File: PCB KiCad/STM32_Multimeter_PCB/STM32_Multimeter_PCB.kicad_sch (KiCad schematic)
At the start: 18 parts, among them SW1 SW_Push, U1 STM32WB55CGUx, Y1 Crystal 32 MHz

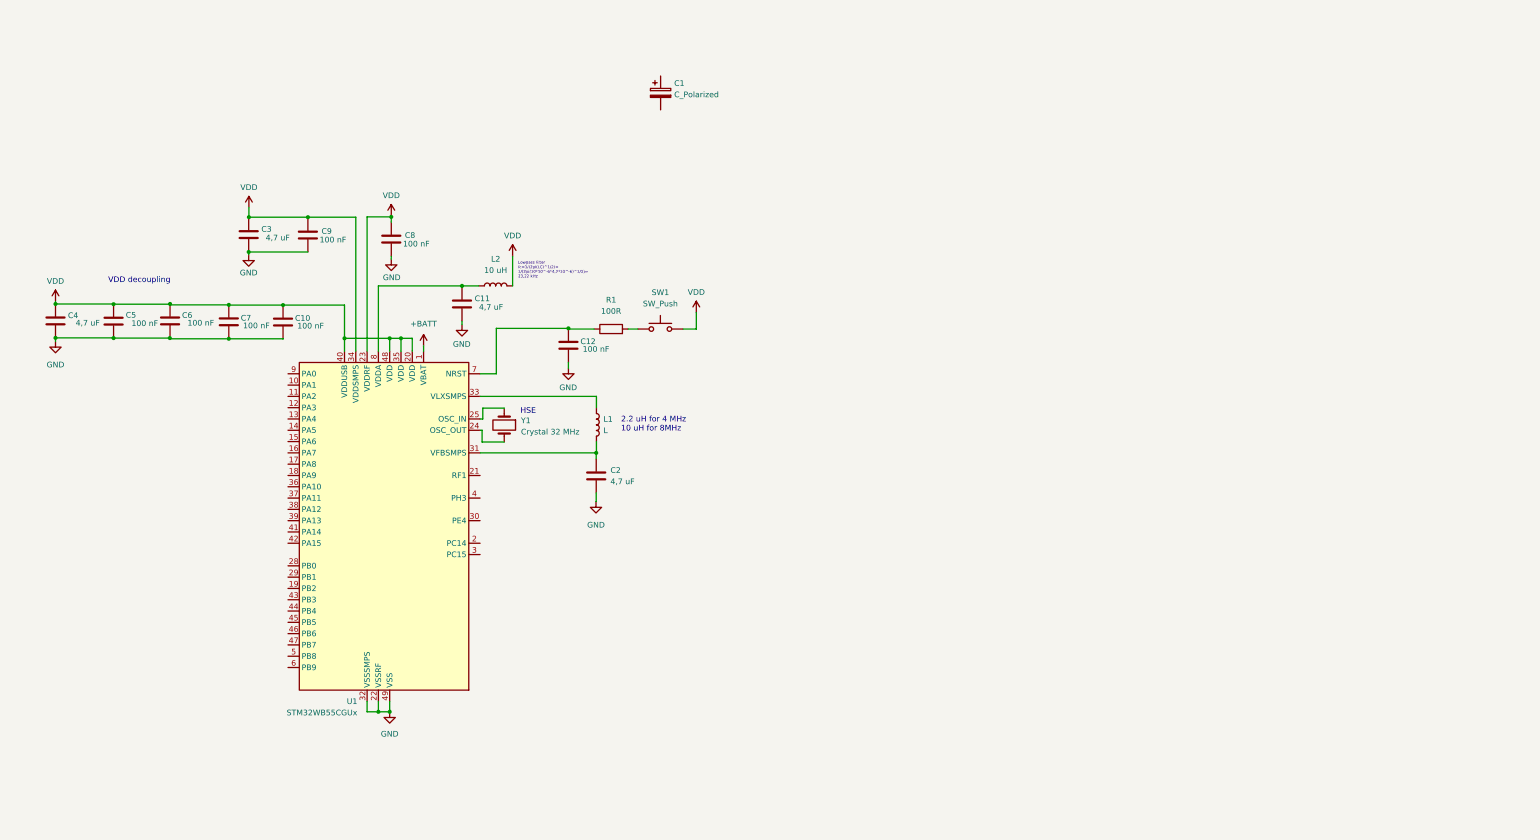
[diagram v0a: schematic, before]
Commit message: Added battery charger/protection, 3,3v buck/boost regualtor andUSB connector
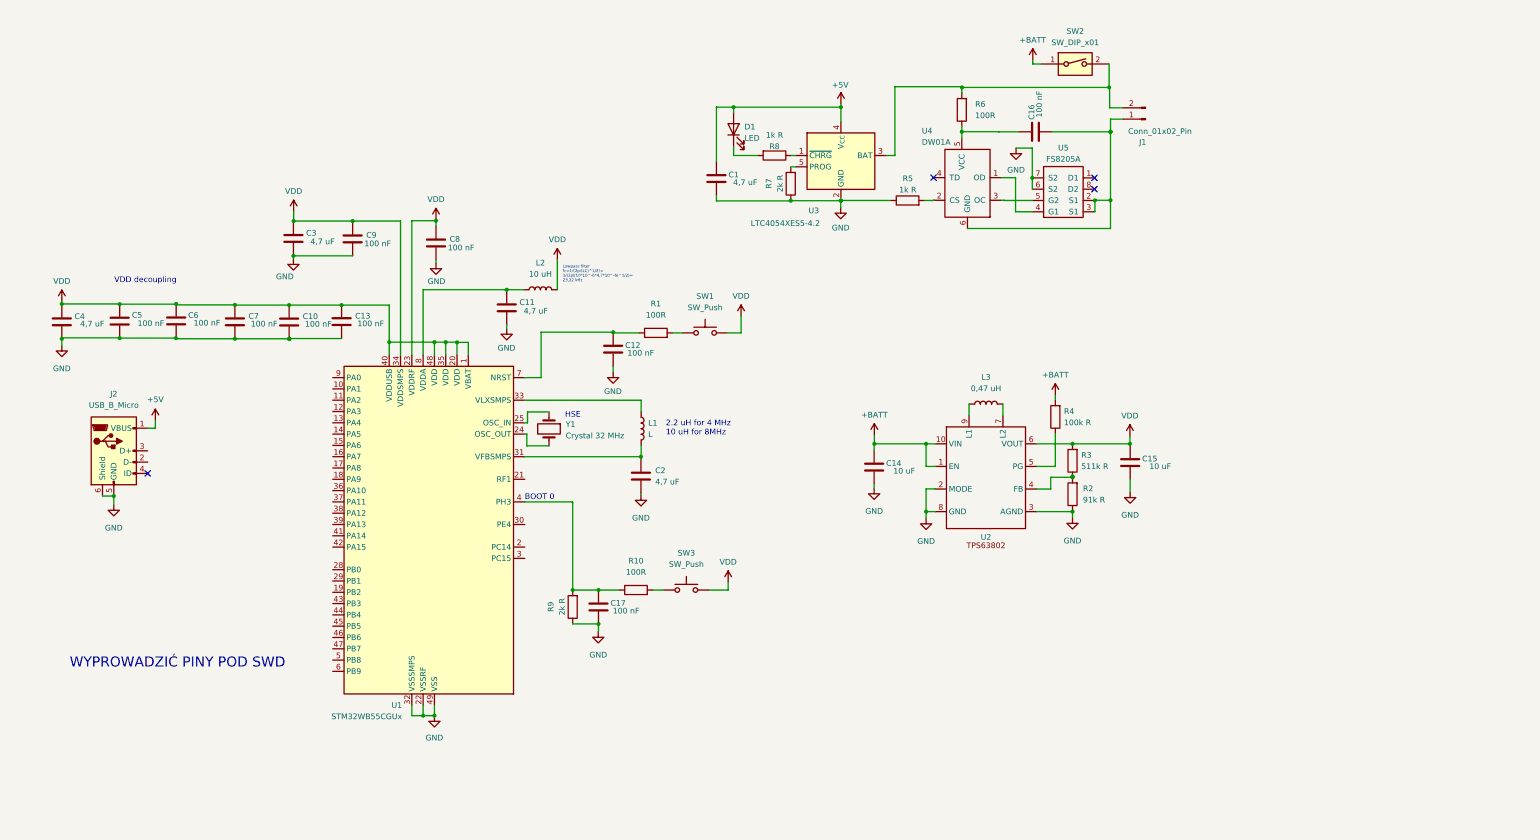
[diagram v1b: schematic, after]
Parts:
- removed C1: C_Polarized, symbol Device:C_Polarized
- added C1: 4,7 uF, symbol Device:C
- added C13, C16, C17: 100 nF, symbol Device:C
- added C14, C15: 10 uF, symbol Device:C
- added D1: LED, symbol Device:LED
- added J1: Conn_01x02_Pin, symbol Connector:Conn_01x02_Pin
- added J2: USB_B_Micro, symbol Connector:USB_B_Micro
- added L3: 0,47 uH, symbol Device:L
- added R10, R6: 100R, symbol Device:R
- added R2: 91k R, symbol Device:R
- added R3: 511k R, symbol Device:R
- added R4: 100k R, symbol Device:R
- added R5, R8: 1k R, symbol Device:R
- added R7, R9: 2k R, symbol Device:R
- added SW2: SW_DIP_x01, symbol Switch:SW_DIP_x01
- added SW3: SW_Push, symbol Switch:SW_Push
- added U2: ~, symbol STM32_Bsed_Meter_Library:TSP63805
- added U3: LTC4054XES5-4.2, Package_TO_SOT_SMD:TSOT-23-5, symbol Battery_Management:LTC4054XES5-4.2
- added U4: DW01A, Package_TO_SOT_SMD:SOT-23-6, symbol dw01a:DW01A
- added U5: FS8205A, Package_SO:TSSOP-8_4.4x3mm_P0.65mm, symbol fs8205a:FS8205A
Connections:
- net +BATT: now also C14.2, R4.2, SW2.1, U2.1 (EN), U2.10 (VIN); no longer U1.1 (VBAT)
- net GND: now also C1.1, C13.1, C14.1, C15.1, C17.1, J2.5 (GND), J2.6 (Shield), R2.1, R5.1, R7.1, R9.1, U2.2 (MODE), U2.3 (AGND), U2.8 (GND), U3.2 (GND), U5.6 (S2), U5.7 (S2)
- net VDD: now also U1.1 (VBAT), C13.2, C15.2, R3.2, SW3.2, U2.6 (VOUT)
- net at U1.4 (PH3): now also C17.2, R10.1, R9.2
- new net: J1.2 (Pin_2), R6.2, SW2.2, U3.3 (BAT)
- new net: C16.1, J1.1 (Pin_1), U4.6 (GND), U5.2 (S1), U5.3 (S1)
- new net: R7.2, U3.5 (PROG)
- new net: R10.2, SW3.1
- new net: R2.2, R3.1, U2.4 (FB)
- new net: D1.1 (K), R8.2
- new net: R8.1, U3.1 (~{CHRG})
- new net: R4.1, U2.5 (PG)
- new net: L3.2, U2.7 (L2)
- new net: L3.1, U2.9 (L1)
- new net: C16.2, R6.1, U4.5 (VCC)
- new net: U4.1 (OD), U5.4 (G1)
- new net: U4.3 (OC), U5.5 (G2)
- new net: R5.2, U4.2 (CS)
- new net +5V: C1.2, D1.2 (A), J2.1 (VBUS), U3.4 (V_{CC})
- no-connect marks 0 -> 4
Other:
- note added: "BOOT 0"
- note added: "WYPROWADZIĆ PINY POD SWD"
- moved on the sheet: C10, C11, C12, C2, C3, C4, C5, C6, C7, C8, C9, L1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

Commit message: Added mcu connectivity: SWD, USB, UART and BLE with supporting circuitry
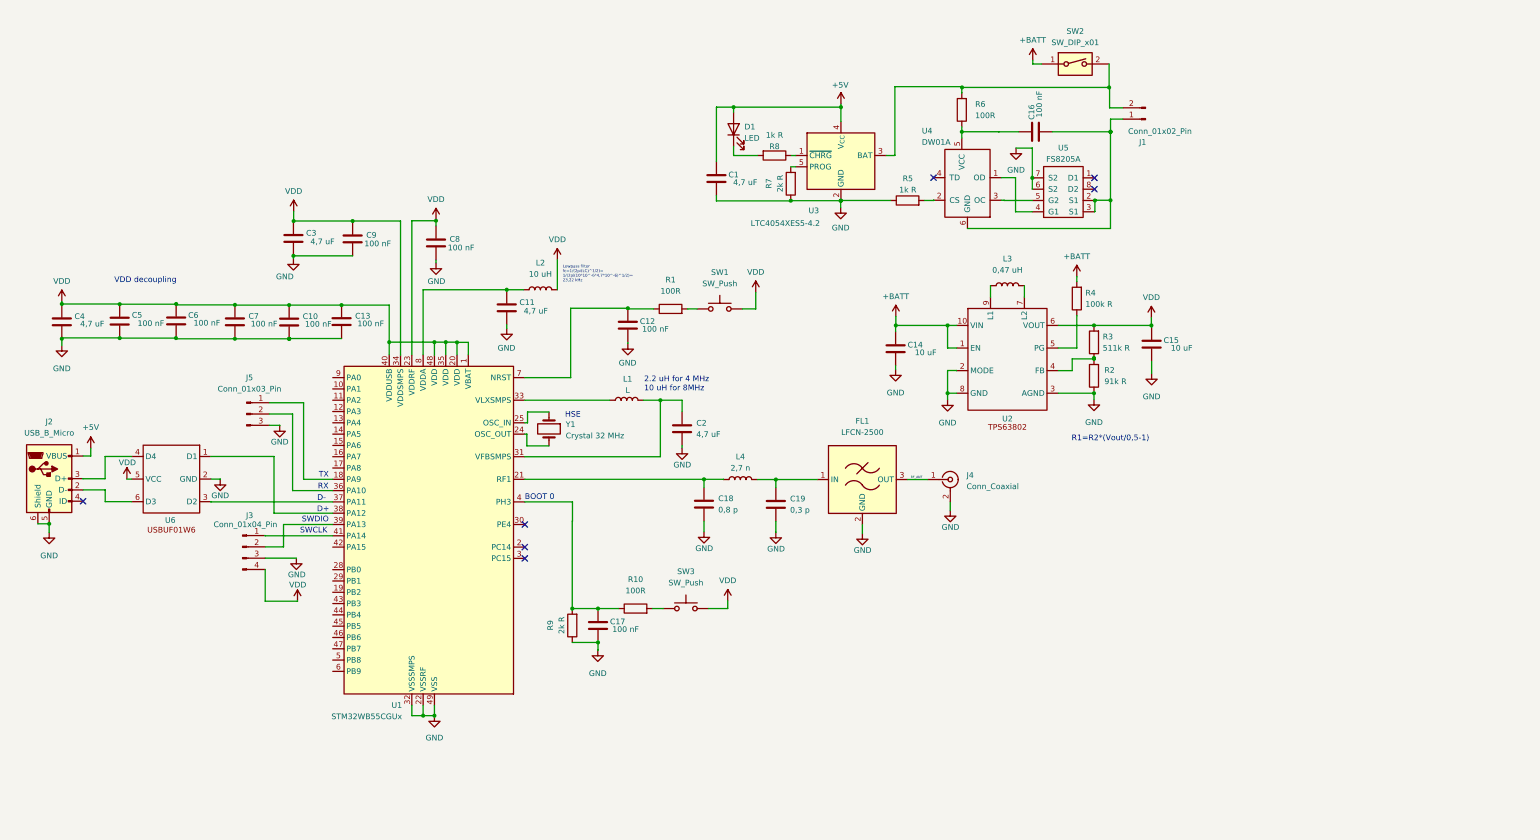
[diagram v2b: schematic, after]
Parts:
- added C18: 0,8 p, symbol Device:C
- added C19: 0,3 p, symbol Device:C
- added FL1: LFCN-2500, Filter:Filter_Mini-Circuits_FV1206, symbol RF_Filter:LFCN-2500
- added J3: Conn_01x04_Pin, symbol Connector:Conn_01x04_Pin
- added J4: Conn_Coaxial, Connector_Coaxial:U.FL_Molex_MCRF_73412-0110_Vertical, symbol Connector:Conn_Coaxial
- added J5: Conn_01x03_Pin, symbol Connector:Conn_01x03_Pin
- added L4: 2,7 n, symbol Device:L
- added U6: ~, symbol STM32_Bsed_Meter_Library:USBUF01W6
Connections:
- net GND: now also C18.2, C19.2, FL1.2 (GND), FL1.4 (GND), J3.3 (Pin_3), J4.2 (Ext), J5.3 (Pin_3), U6.2 (GND)
- net VDD: now also J3.4 (Pin_4), U6.5 (VCC)
- net at U1.18 (PA9): now also J5.1 (Pin_1)
- net at U1.21 (RF1): now also C18.1, L4.1
- net at U1.36 (PA10): now also J5.2 (Pin_2)
- net at U1.37 (PA11): now also U6.3 (D2)
- net at U1.38 (PA12): now also U6.1 (D1)
- net at U1.39 (PA13): now also J3.2 (Pin_2)
- net at U1.41 (PA14): now also J3.1 (Pin_1)
- net at J2.2 (D-): now also U6.6 (D3)
- net at J2.3 (D+): now also U6.4 (D4)
- new net: C19.1, FL1.1 (IN), L4.2
- new net: FL1.3 (OUT), J4.1 (In)
- no-connect marks 4 -> 7
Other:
- note added: "D+"
- note added: "D-"
- note added: "R1=R2*(Vout/0,5-1)"
- note added: "RX"
- note added: "SWCLK"
- note added: "SWDIO"
- note added: "TX"
- note removed: "WYPROWADZIĆ PINY POD SWD"
- moved on the sheet: C12, C14, C15, C17, C2, J2, L1, L3, R1, R10, R2, R3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

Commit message: Added voltage and current sensing input
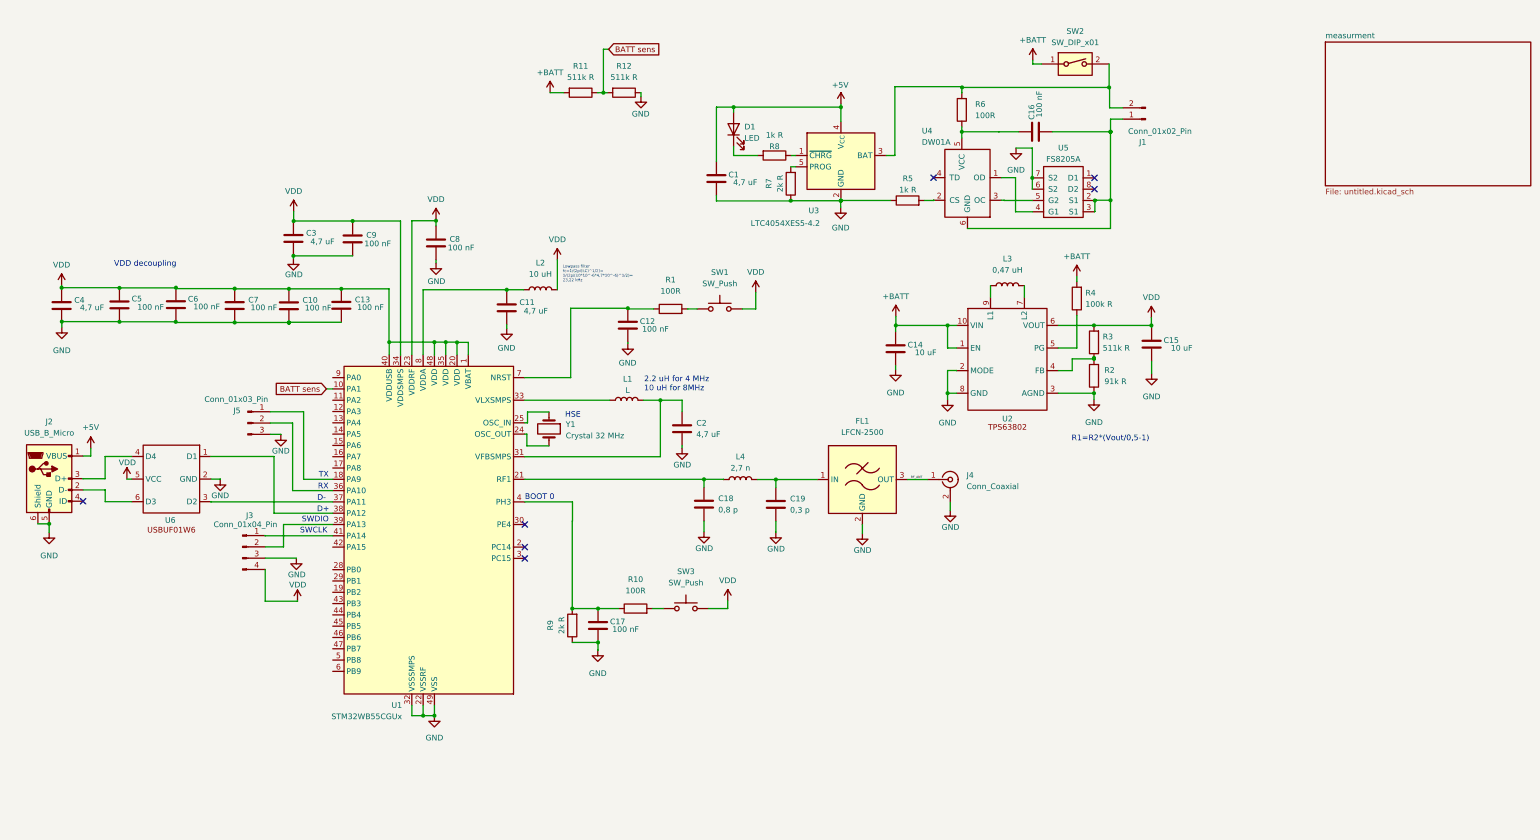
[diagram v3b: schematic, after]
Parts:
- added R11, R12: 511k R, symbol Device:R
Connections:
- net +BATT: now also R11.2
- net GND: now also R12.1
- net BATT sens: now reaches U1.10 (PA1)
- net BATT sens: now also R11.1, R12.2
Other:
- added sheet measurment (untitled.kicad_sch)
- moved on the sheet: C10, C13, C4, C5, C6, C7, J5

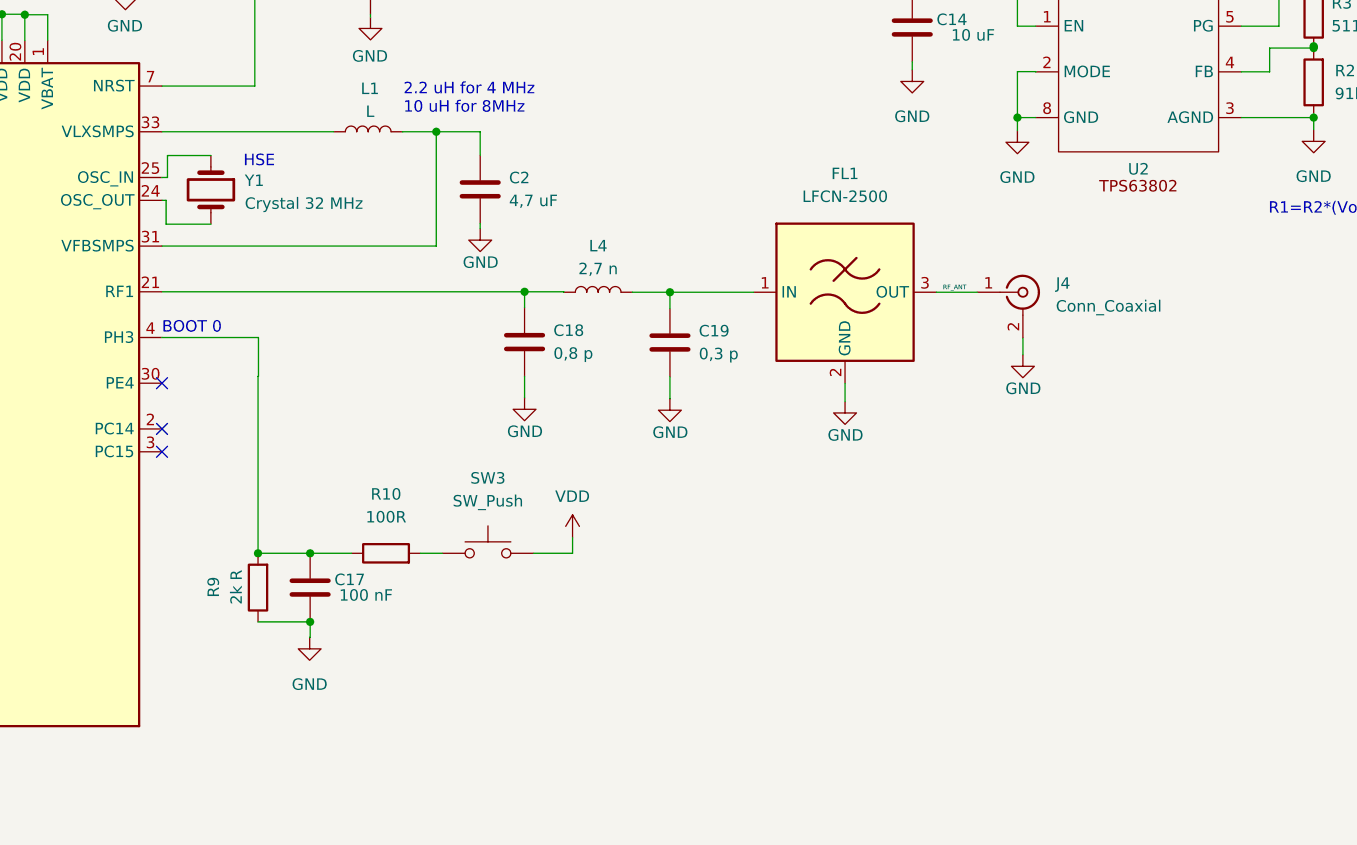
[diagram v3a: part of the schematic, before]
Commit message: Changed RF filter
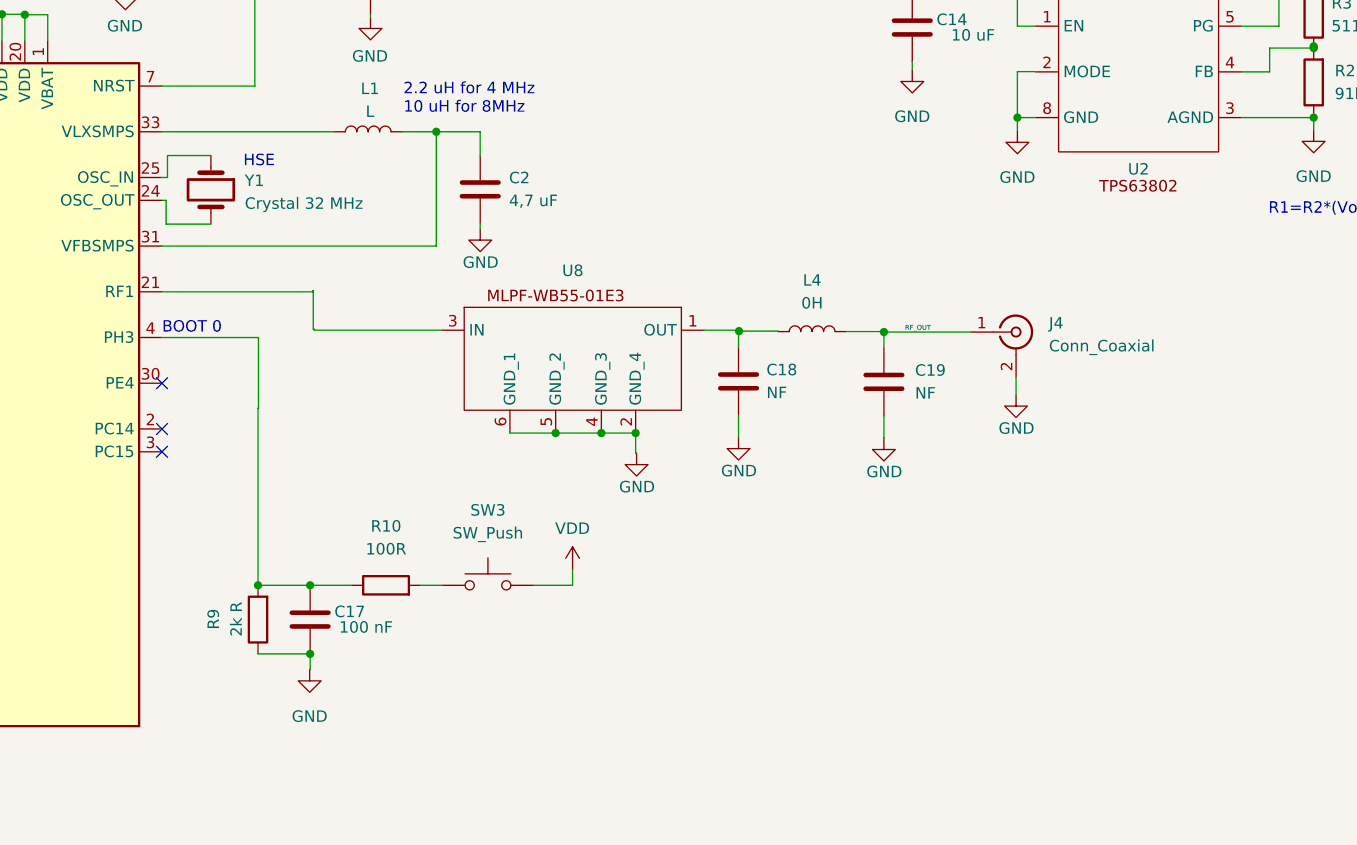
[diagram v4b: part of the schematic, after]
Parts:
- removed FL1: LFCN-2500, Filter:Filter_Mini-Circuits_FV1206, symbol RF_Filter:LFCN-2500
- added U8: ~, symbol STM32_Bsed_Meter_Library:MLPF_WB55_e01e3
- C18: value 0,8 p -> NF
- C19: value 0,3 p -> NF
- L4: value 2,7 n -> 0H
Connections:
- net GND: now also U8.2 (GND_4), U8.4 (GND_3), U8.5 (GND_2), U8.6 (GND_1)
- net at C18.1, L4.1: now also U8.1 (OUT); no longer U1.21 (RF1)
- net at C19.1, L4.2: now also J4.1 (In)
- new net: U1.21 (RF1), U8.3 (IN)
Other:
- moved on the sheet: C17, C18, C19, J4, L4, R10, R9, SW3
